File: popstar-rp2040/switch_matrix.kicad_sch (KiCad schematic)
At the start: 151 parts, among them SW10 MX_SW_solder, SW11 MX_SW_solder, SW12 MX_SW_solder, SW13 MX_SW_solder, SW14 MX_SW_solder, SW15 MX_SW_solder, SW16 MX_SW_solder, SW17 MX_SW_solder, SW18 MX_SW_solder, SW19 MX_SW_solder, SW2 MX_SW_solder, SW20 MX_SW_solder, SW21 MX_SW_solder, SW22 MX_SW_solder, SW23 MX_SW_solder, SW24 MX_SW_solder, SW25 MX_SW_solder, SW26 MX_SW_solder, SW27 MX_SW_solder, SW28 MX_SW_solder, SW29 MX_SW_solder, SW3 MX_SW_solder, SW30 MX_SW_solder, SW31 MX_SW_solder, SW32 MX_SW_solder, SW33 MX_SW_solder, SW34 MX_SW_solder, SW35 MX_SW_solder, SW36 MX_SW_solder, SW37 MX_SW_solder, SW38 MX_SW_solder, SW39 MX_SW_solder, SW4 MX_SW_solder, SW40 MX_SW_solder, SW41 MX_SW_solder, SW42 MX_SW_solder, SW43 MX_SW_solder, SW44 MX_SW_solder, SW45 MX_SW_solder, SW46 MX_SW_solder, SW47 MX_SW_solder, SW48 MX_SW_solder, SW49 MX_SW_solder, SW5 MX_SW_solder, SW50 MX_SW_solder, SW51 MX_SW_solder, SW52 MX_SW_solder, SW53 MX_SW_solder, SW54 MX_SW_solder, SW55 MX_SW_solder, SW56 MX_SW_solder, SW57 MX_SW_solder, SW58 MX_SW_solder, SW59 MX_SW_solder, SW6 MX_SW_solder, SW60 MX_SW_solder, SW61 MX_SW_solder, SW62 MX_SW_solder, SW7 MX_SW_solder, SW8 MX_SW_solder, SW9 MX_SW_solder, U5 74AHCT1G125

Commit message: Correct 2.25 left shift to use 2.25 stab footprint
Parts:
- S4: footprint marbastlib-mx:STAB_MX_P_6.25u -> marbastlib-mx:STAB_MX_2.25u
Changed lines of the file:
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@@
       (effects (font (size 1.27 1.27)) (justify left))
     )
-    (property "Footprint" "marbastlib-mx:STAB_MX_P_6.25u" (at 20.32 81.28 0)
+    (property "Footprint" "marbastlib-mx:STAB_MX_2.25u" (at 20.32 81.28 0)
       (effects (font (size 1.27 1.27)) hide)
     )

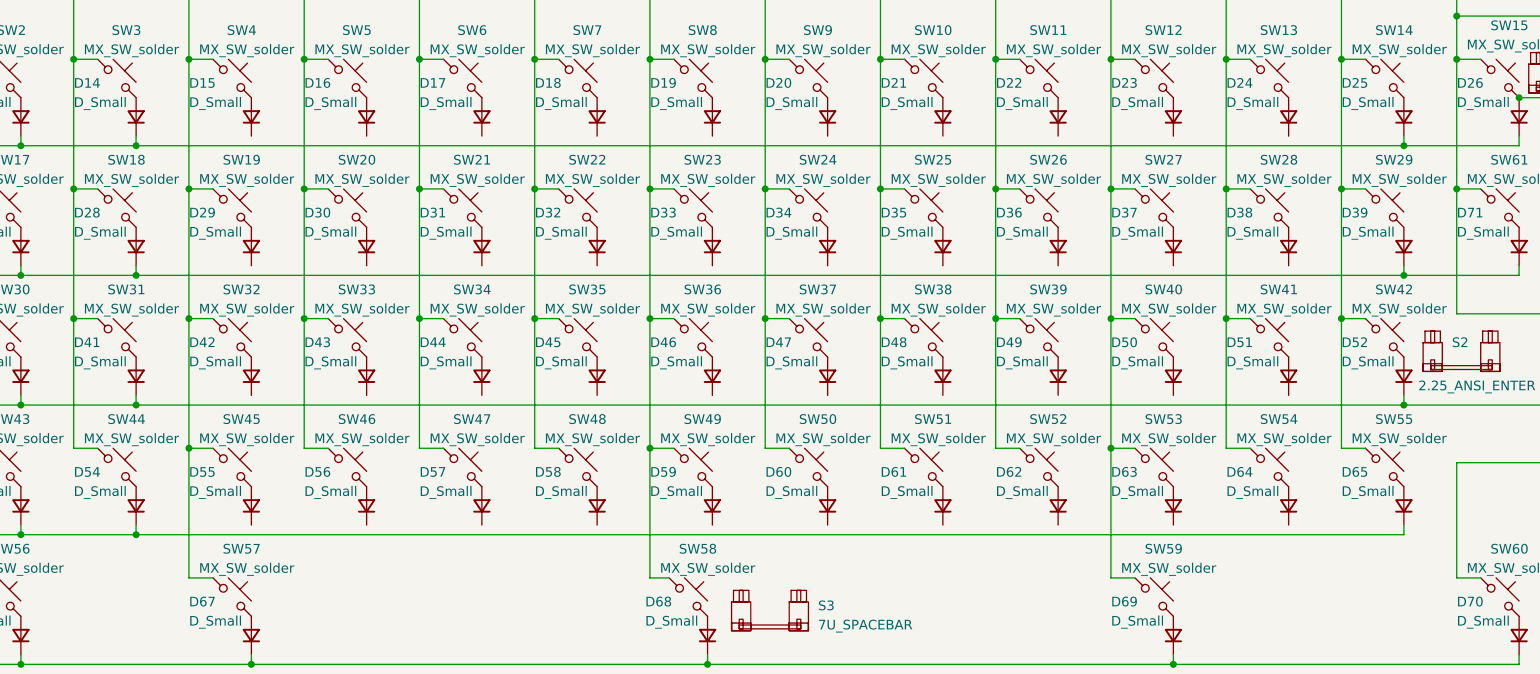
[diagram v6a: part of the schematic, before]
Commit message: Properly connected diodes to switches in the schematic
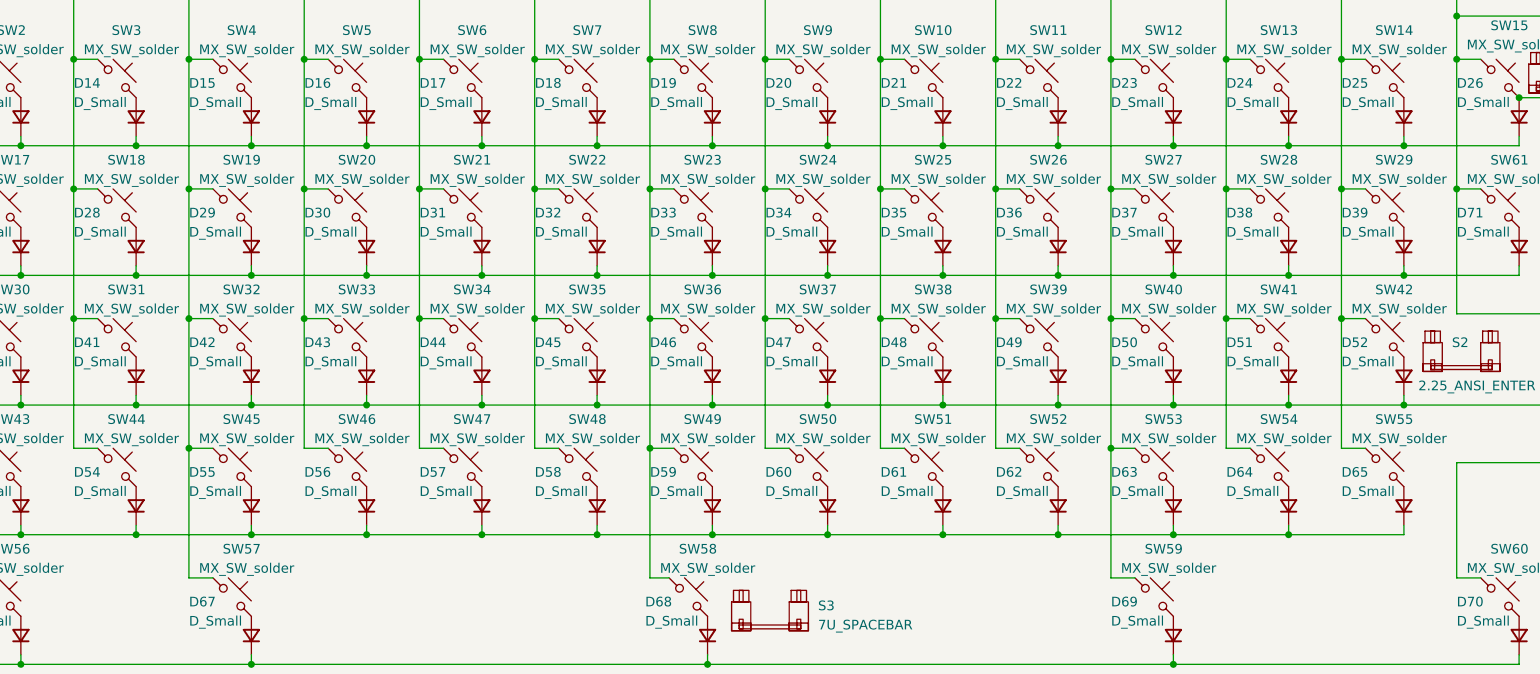
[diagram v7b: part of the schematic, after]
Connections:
- net ROW0: now also D15.1 (K), D16.1 (K), D17.1 (K), D18.1 (K), D19.1 (K), D20.1 (K), D21.1 (K), D22.1 (K), D23.1 (K), D24.1 (K)
- net ROW1: now also D29.1 (K), D30.1 (K), D31.1 (K), D32.1 (K), D33.1 (K), D34.1 (K), D35.1 (K), D36.1 (K), D37.1 (K), D38.1 (K)
- net ROW2: now also D42.1 (K), D43.1 (K), D44.1 (K), D45.1 (K), D46.1 (K), D47.1 (K), D48.1 (K), D49.1 (K), D50.1 (K), D51.1 (K)
- net ROW3: now also D55.1 (K), D56.1 (K), D57.1 (K), D58.1 (K), D59.1 (K), D60.1 (K), D61.1 (K), D62.1 (K), D63.1 (K), D64.1 (K)

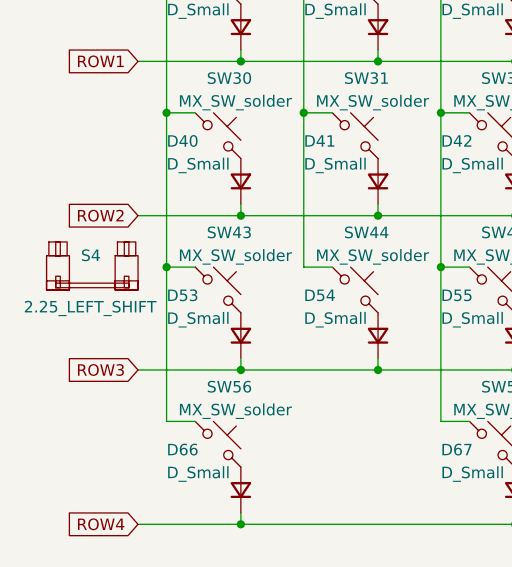
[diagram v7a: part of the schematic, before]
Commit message: Fixed footprint mismatch for stabs
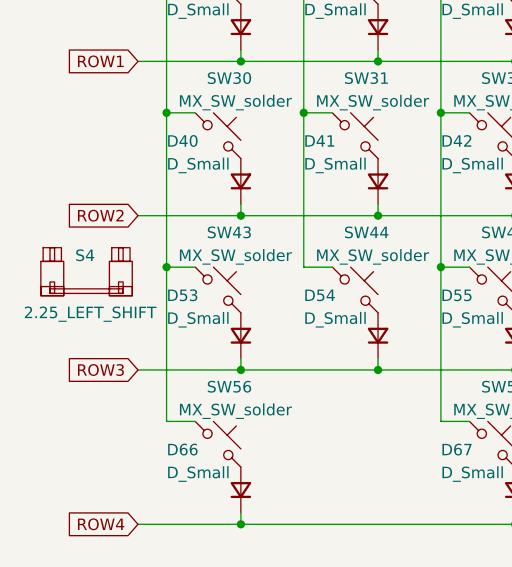
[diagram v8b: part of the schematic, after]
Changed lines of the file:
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@@
-    )
-  )
-  (symbol (lib_id "marbastlib-mx:MX_stab") (at 20.32 81.28 0) (unit 1)
-    (in_bom yes) (on_board yes) (dnp no)
-    (property "Reference" "S4" (at 19.05 80.01 0)
-      (effects (font (size 1.27 1.27)) (justify left))
-    )
-    (property "Value" "2.25_LEFT_SHIFT" (at 12.7 85.725 0)
-      (effects (font (size 1.27 1.27)) (justify left))
-    )
-    (property "Footprint" "marbastlib-mx:STAB_MX_2.25u" (at 20.32 81.28 0)
-      (effects (font (size 1.27 1.27)) hide)
-    )
-    (property "Datasheet" "" (at 20.32 81.28 0)
-      (effects (font (size 1.27 1.27)) hide)
-    )
-    (instances
-      (project "popstar"
-        (path "/2b78fc64-feb6-4bfa-a478-e5c73a3e42a2/7b7e0ca3-1d6a-48a7-b8ef-32a16011b189"
-          (reference "S4") (unit 1)
-        )
-      )
     )
   )
@@
         )
       )
+    )
+  )
+  (symbol (lib_id "marbastlib-mx:MX_stab") (at 19.685 81.915 0) (unit 1)
+    (in_bom yes) (on_board yes) (dnp no)
+    (property "Reference" "S4" (at 18.415 80.01 0)
+      (effects (font (size 1.27 1.27)) (justify left))
+    )
+    (property "Value" "2.25_LEFT_SHIFT" (at 12.7 86.36 0)
+      (effects (font (size 1.27 1.27)) (justify left))
+    )
+    (property "Footprint" "marbastlib-mx:STAB_MX_2.25u" (at 19.685 81.915 0)
+      (effects (font (size 1.27 1.27)) hide)
+    )
+    (property "Datasheet" "" (at 19.685 81.915 0)
+      (effects (font (size 1.27 1.27)) hide)
+    )
+    (instances
+      (project "popstar"
+        (path "/2b78fc64-feb6-4bfa-a478-e5c73a3e42a2/7b7e0ca3-1d6a-48a7-b8ef-32a16011b189"
+          (reference "S4") (unit 1)
+        )
+      )
